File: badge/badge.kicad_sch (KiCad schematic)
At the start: 20 parts, among them J1 Conn_02x03_Odd_Even, U1 ATtiny424-SSU

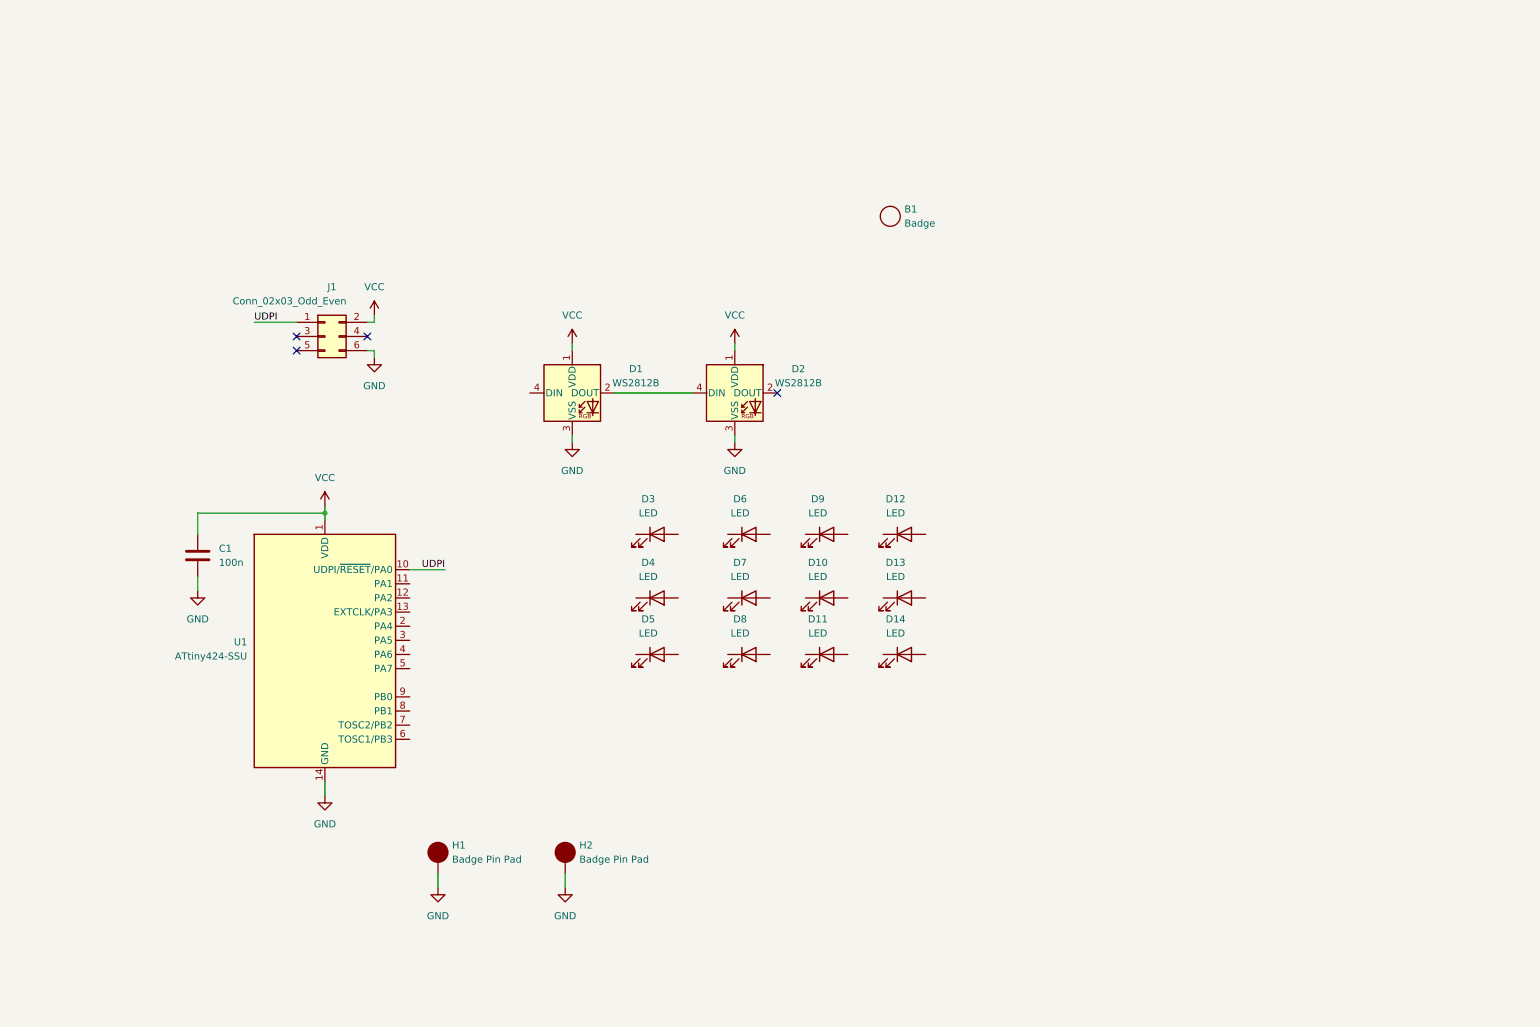
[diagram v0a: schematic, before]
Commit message: schematic nearlly finished + new design on inkscape
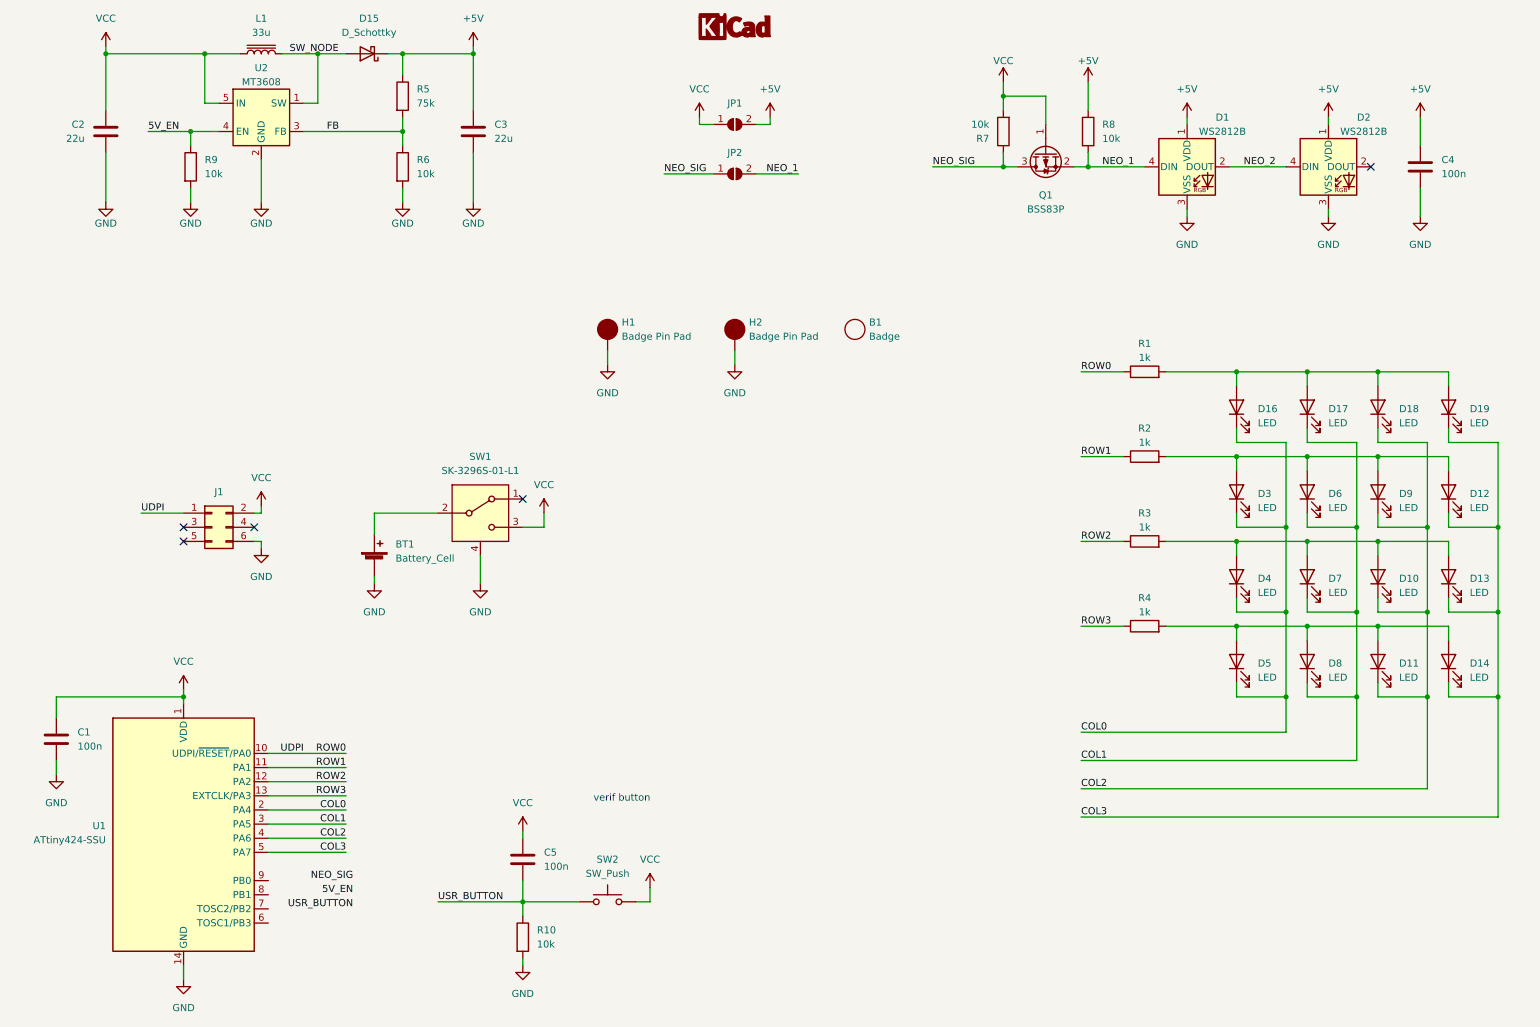
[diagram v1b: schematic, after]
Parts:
- added BT1: Battery_Cell, badge:cr_2032_holder_S8421-45R, symbol Device:Battery_Cell
- added C2, C3: 22u, Resistor_SMD:R_1206_3216Metric_Pad1.30x1.75mm_HandSolder, symbol Device:C
- added C4, C5: 100n, Resistor_SMD:R_0805_2012Metric_Pad1.20x1.40mm_HandSolder, symbol Device:C
- added D15: D_Schottky, Diode_SMD:D_SMA, symbol Device:D_Schottky
- added D16, D17, D18, D19: LED, badge:LED_0805_2012_badge, symbol Device:LED
- added G1: KiCAD LOGO Small, Symbol:Symbol_CC-Attribution_CopperTop_Small, symbol guigur-lib:KiCAD LOGO Small
- added JP1, JP2: SolderJumper_2_Open, Jumper:SolderJumper-2_P1.3mm_Open_TrianglePad1.0x1.5mm, symbol Jumper:SolderJumper_2_Open
- added L1: 33u, Inductor_SMD:L_6.3x6.3_H3, symbol Device:L_Iron
- added Q1: BSS83P, Package_TO_SOT_SMD:SOT-23, symbol Transistor_FET:BSS83P
- added R1, R2, R3, R4: 1k, Resistor_SMD:R_0603_1608Metric_Pad0.98x0.95mm_HandSolder, symbol Device:R
- added R10, R6, R7, R8, R9: 10k, Resistor_SMD:R_0603_1608Metric_Pad0.98x0.95mm_HandSolder, symbol Device:R
- added R5: 75k, Resistor_SMD:R_0603_1608Metric_Pad0.98x0.95mm_HandSolder, symbol Device:R
- added SW1: SK-3296S-01-L1, badge:sk-3296s-01-l1, symbol badge-lib:SK-3296S-01-L1
- added SW2: SW_Push, Button_Switch_SMD:SW_Push_1P1T_NO_CK_KSC6xxJ, symbol Switch:SW_Push
- added U2: MT3608, Package_TO_SOT_SMD:SOT-23-6, symbol Regulator_Switching:MT3608
- D10, D11, D12, D13, D14, D3, D4, D5, D6, D7, D8, D9: footprint LED_SMD:LED_0805_2012Metric_Pad1.15x1.40mm_HandSolder -> badge:LED_0805_2012_badge
- H1, H2: footprint (none) -> badge:pin_badge
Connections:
- net GND: now also BT1.2 (-), C2.2, C3.2, C4.2, R10.2, R6.2, R9.2, SW1.4 (CHASSIS), U2.2 (GND)
- net VCC: now also C2.1, C5.1, JP1.1 (A), L1.1, Q1.1 (G), R7.2, SW1.3 (C), SW2.2, U2.5 (IN); no longer D1.1 (VDD), D2.1 (VDD)
- net COL2: now reaches D11.1 (K)
- net COL2: now also D10.1 (K), D9.1 (K), U1.4 (PA6), D18.1 (K)
- net at D11.2 (A): now also D14.2 (A), D5.2 (A), D8.2 (A), R4.2
- net at D9.2 (A): now also D12.2 (A), D3.2 (A), D6.2 (A), R2.2
- net COL0: now reaches D3.1 (K)
- net COL0: now also D4.1 (K), D5.1 (K), U1.2 (PA4), D16.1 (K)
- net COL1: now reaches D8.1 (K)
- net COL1: now also D6.1 (K), D7.1 (K), U1.3 (PA5), D17.1 (K)
- net NEO_2: now reaches D1.2 (DOUT), D2.4 (DIN)
- net NEO_1: now reaches D1.4 (DIN)
- net NEO_1: now also JP2.2 (B), Q1.2 (S), R8.2
- net COL3: now reaches D14.1 (K)
- net COL3: now also D12.1 (K), D13.1 (K), U1.5 (PA7), D19.1 (K)
- net at D7.2 (A): now also D10.2 (A), D13.2 (A), D4.2 (A), R3.2
- net ROW1: now reaches U1.11 (PA1)
- net ROW1: now also R2.1
- net ROW2: now reaches U1.12 (PA2)
- net ROW2: now also R3.1
- net ROW3: now reaches U1.13 (EXTCLK/PA3)
- net ROW3: now also R4.1
- net UDPI renamed ROW0
- net ROW0: now also R1.1
- new net: BT1.1 (+), SW1.2 (B)
- new net: D16.2 (A), D17.2 (A), D18.2 (A), D19.2 (A), R1.2
- new net +5V: C3.1, C4.1, D1.1 (VDD), D15.1 (K), D2.1 (VDD), JP1.2 (B), R5.1, R8.1
- new net 5V_EN: R9.1, U2.4 (EN)
- new net FB: R5.2, R6.1, U2.3 (FB)
- new net NEO_SIG: JP2.1 (A), Q1.3 (D), R7.1
- new net SW_NODE: D15.2 (A), L1.2, U2.1 (SW)
- new net USR_BUTTON: C5.2, R10.1, SW2.1
- no-connect marks 4 -> 5
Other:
- note added: "verif button"
- moved on the sheet: B1, C1, D1, D10, D11, D12, D13, D14, D2, D3, D4, D5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

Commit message: wip schematic finished and slow fill on pcb. test before removing all tracks
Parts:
- removed C4: 100n, Resistor_SMD:R_0805_2012Metric_Pad1.20x1.40mm_HandSolder, symbol Device:C
- renumbered D16 to D1, D7 to D10, D10 to D11, D13 to D12, D5 to D13, D8 to D14, D11 to D15, D14 to D16, D15 to D17, D1 to D18, D2 to D19, D17 to D2, D18 to D3, D19 to D4, D3 to D5, D9 to D7, D12 to D8, D4 to D9
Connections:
- net 5V_EN: now also U1.9 (PB0)
- net NEO_SIG: now also U1.8 (PB1)
- net ROW0: now also U1.13 (EXTCLK/PA3); no longer J1.1 (Pin_1), U1.10 (UDPI/~{RESET}/PA0)
- net ROW1: now also U1.12 (PA2); no longer U1.11 (PA1)
- net ROW2: now also U1.11 (PA1); no longer U1.12 (PA2)
- net USR_BUTTON: now also U1.7 (TOSC2/PB2)
- net R1: now reaches D5.2 (A), D6.2 (A), D7.2 (A), D8.2 (A), R2.2
- net R3: now reaches D13.2 (A), D14.2 (A), D15.2 (A), D16.2 (A), R4.2
- net R0: now reaches D1.2 (A), D2.2 (A), D3.2 (A), D4.2 (A), R1.2
- net R2: now reaches D10.2 (A), D11.2 (A), D12.2 (A), D9.2 (A), R3.2
- net ROW3 renamed UDPI/ROW3
- net UDPI/ROW3: now also J1.1 (Pin_1), U1.10 (UDPI/~{RESET}/PA0); no longer U1.13 (EXTCLK/PA3)
- no-connect marks 5 -> 6
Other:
- moved on the sheet: BT1, C5, D18, D19, J1, Q1, R10, R7, R8, SW1, SW2

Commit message: finished the led matrix
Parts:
- removed JP1: SolderJumper_2_Open, Jumper:SolderJumper-2_P1.3mm_Open_TrianglePad1.0x1.5mm, symbol Jumper:SolderJumper_2_Open
- added JP10, JP11, JP12, JP14, JP15, JP16, JP2, JP3, JP4: 0, badge:R_1206_3216_jumper, symbol Device:R_Small
- added JP17: 0, Resistor_SMD:R_1206_3216Metric_Pad1.30x1.75mm_HandSolder, symbol Device:R
- G1: footprint Symbol:Symbol_CC-Attribution_CopperTop_Small -> Symbol:KiCad-Logo2_5mm_SilkScreen
- R1, R2, R3, R4: footprint Resistor_SMD:R_0603_1608Metric_Pad0.98x0.95mm_HandSolder -> badge:R_1206_3216_jumper
- renumbered JP2 to JP18
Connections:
- net COL0: now also U1.5 (PA7); no longer U1.2 (PA4)
- net COL1: now also U1.4 (PA6), JP10.2, JP14.2, JP2.2; no longer D10.1 (K), D14.1 (K), D2.1 (K), U1.3 (PA5)
- net COL2: now also U1.3 (PA5), JP11.2, JP15.2, JP3.2; no longer D11.1 (K), D15.1 (K), D3.1 (K), U1.4 (PA6)
- net COL3: now also U1.2 (PA4), JP12.2, JP16.2, JP4.2; no longer D12.1 (K), D16.1 (K), D4.1 (K), U1.5 (PA7)
- net GND: now also B1.1
- net VCC: now also JP17.2; no longer SW1.3 (C)
- net at SW1.2 (B): now also JP17.1; no longer BT1.1 (+)
- new net: BT1.1 (+), SW1.3 (C)
- new net: D15.1 (K), JP15.1
- new net: D14.1 (K), JP14.1
- new net: D2.1 (K), JP2.1
- new net: D11.1 (K), JP11.1
- new net: D3.1 (K), JP3.1
- new net: D4.1 (K), JP4.1
- new net: D16.1 (K), JP16.1
- new net: D10.1 (K), JP10.1
- new net: D12.1 (K), JP12.1
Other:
- moved on the sheet: D1, D10, D11, D12, D13, D14, D15, D16, D2, D3, D4, D6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

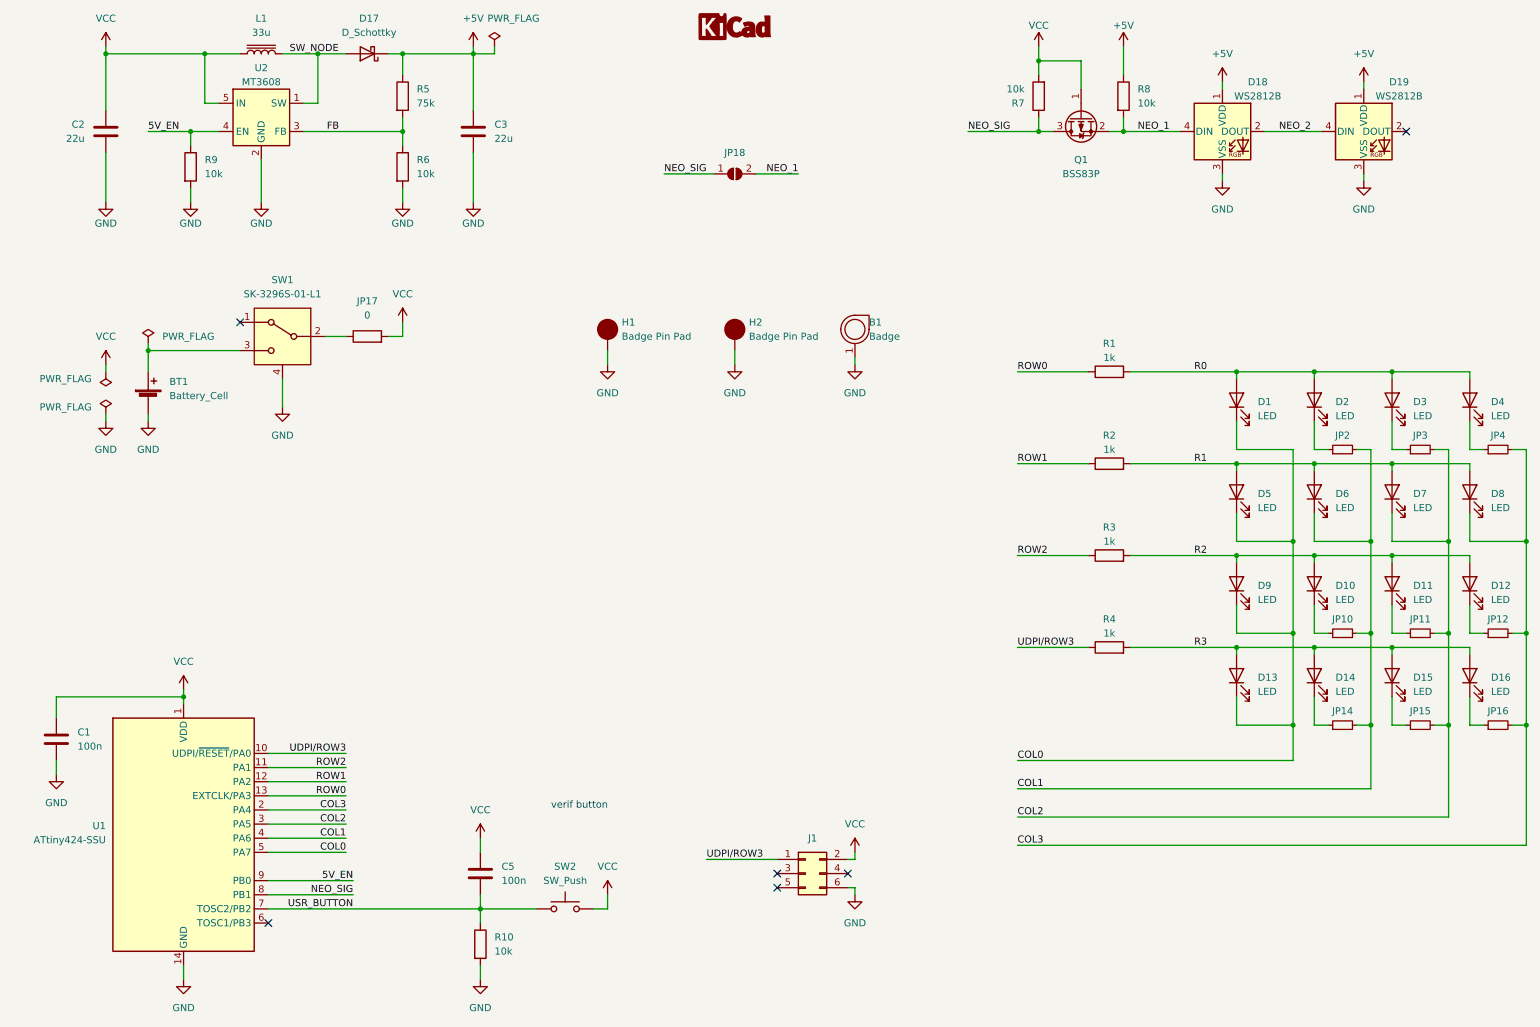
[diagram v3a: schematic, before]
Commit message: routing finished. need to update one last time the badge's footprint tho
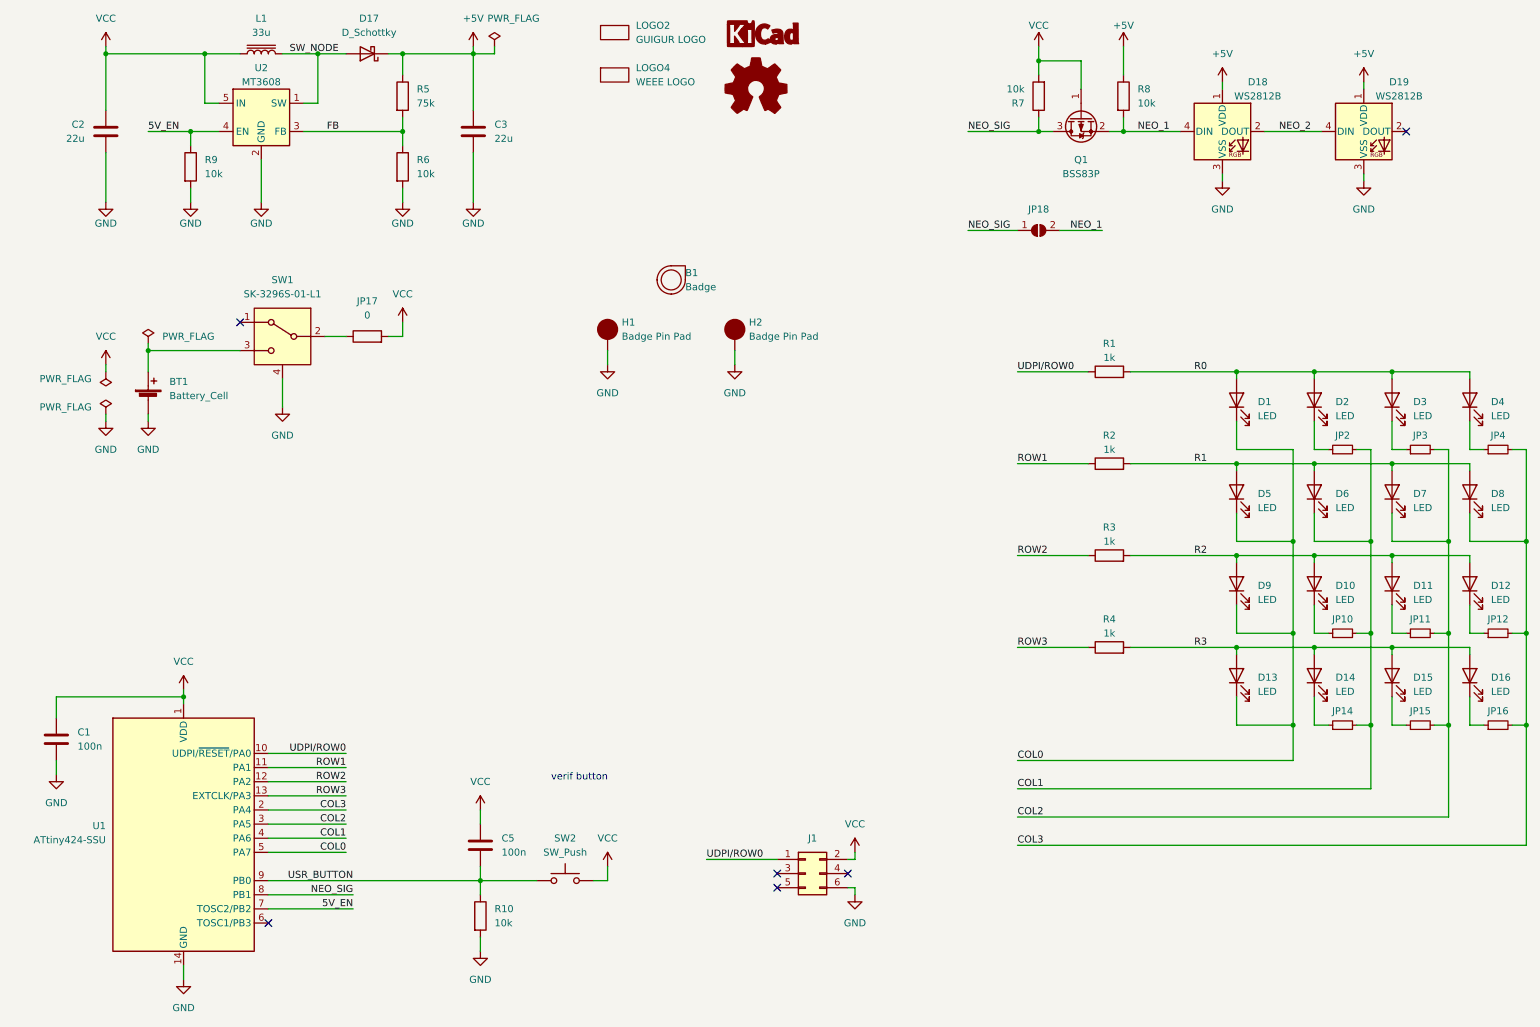
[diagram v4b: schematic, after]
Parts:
- added LOGO1: Logo_Open_Hardware_Small, Symbol:OSHW-Logo2_7.3x6mm_SilkScreen, symbol Graphic:Logo_Open_Hardware_Small
- added LOGO2: GUIGUR LOGO, guigur-lib:guigur_engineering_extra_small_logo, symbol guigur-lib:LOGO
- added LOGO4: WEEE LOGO, Symbol:WEEE-Logo_4.2x6mm_SilkScreen, symbol guigur-lib:LOGO
- C5: footprint Resistor_SMD:R_0805_2012Metric_Pad1.20x1.40mm_HandSolder -> Capacitor_SMD:C_0805_2012Metric_Pad1.18x1.45mm_HandSolder
- L1: footprint Inductor_SMD:L_6.3x6.3_H3 -> Inductor_SMD:L_Bourns-SRN4018
- LOGO3: renamed from G1; footprint Symbol:KiCad-Logo2_5mm_SilkScreen -> guigur-lib:kicad_design_with_7.5mm
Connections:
- net 5V_EN: now also U1.7 (TOSC2/PB2); no longer U1.9 (PB0)
- net GND: no longer B1.1
- net ROW1: now also U1.11 (PA1); no longer U1.12 (PA2)
- net ROW2: now also U1.12 (PA2); no longer U1.11 (PA1)
- net USR_BUTTON: now also U1.9 (PB0); no longer U1.7 (TOSC2/PB2)
- net ROW0 renamed ROW3
- net ROW3: now also R4.1; no longer R1.1
- net UDPI/ROW3 renamed UDPI/ROW0
- net UDPI/ROW0: now also R1.1; no longer R4.1
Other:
- moved on the sheet: C5, JP18, R10, SW2
